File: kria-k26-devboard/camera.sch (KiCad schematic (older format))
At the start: 16 parts, among them J3 WE_68715014522, U60 AP7340-18FS4-7, U9 PI4MSD5V9540BUEX

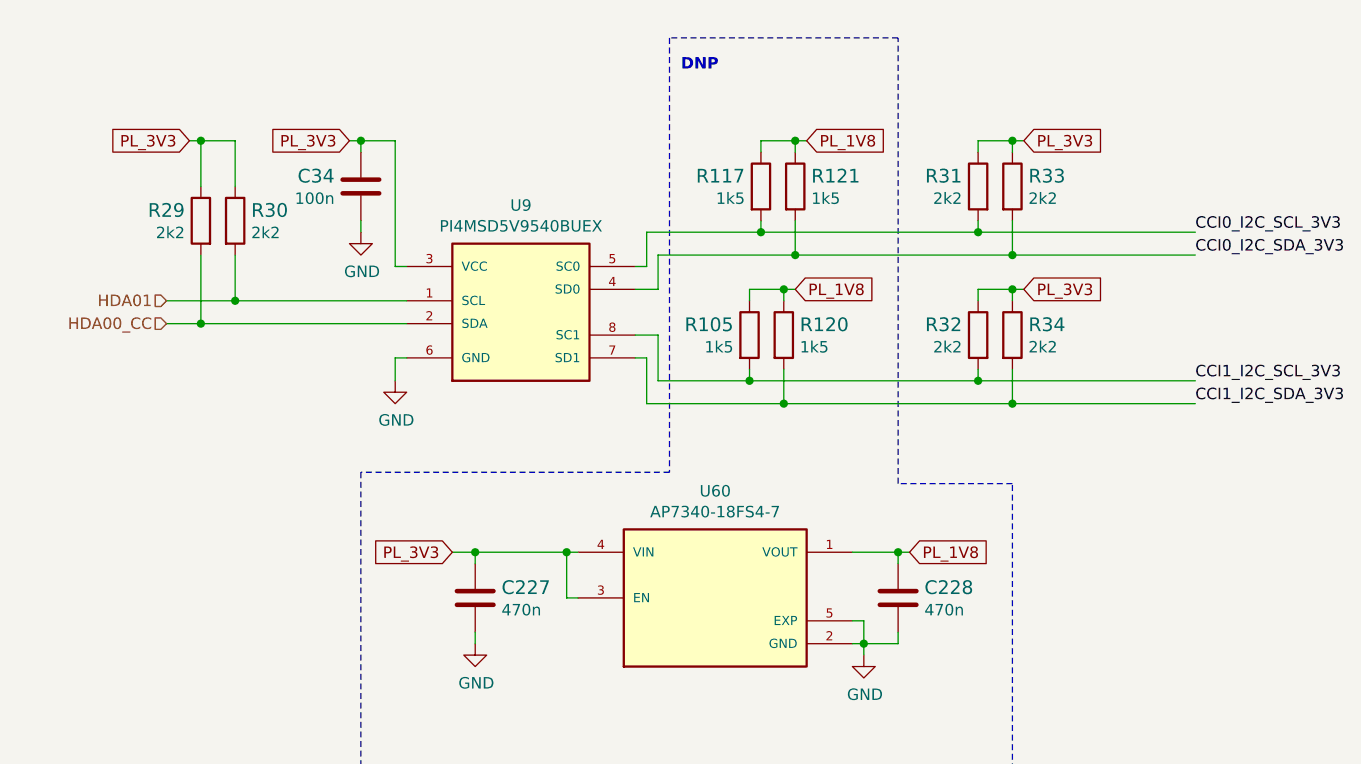
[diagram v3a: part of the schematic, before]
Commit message: Fixed missing USB - M2 connection, finishing touches of PCB
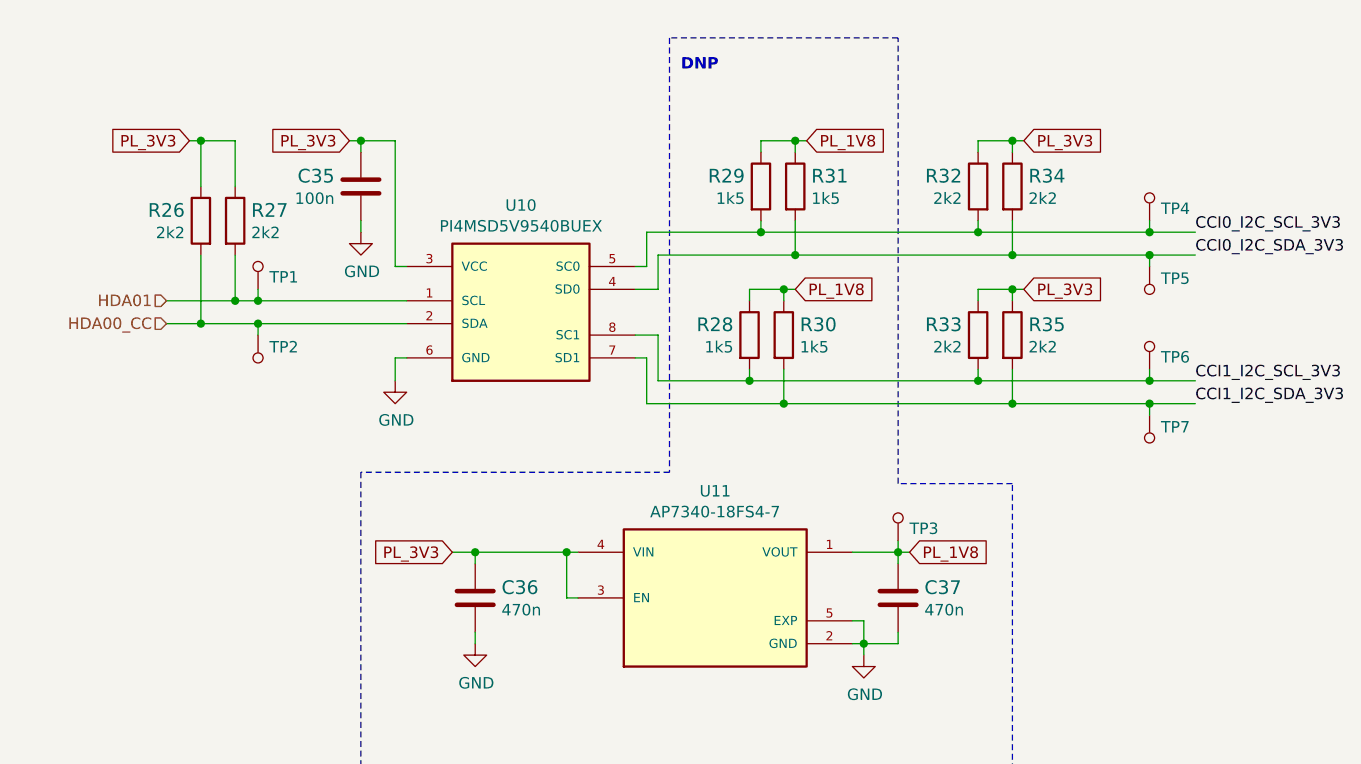
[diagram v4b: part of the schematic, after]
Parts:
- added TP1, TP2, TP3, TP4, TP5, TP6, TP7: TP_SMD_0_75MM, antmicro-footprints:Testpoint_smd_0_75mm, symbol antmicroTestPoints:TP_SMD_0_75MM
- renumbered C34 to C35, C227 to C36, C228 to C37, R29 to R26, R30 to R27, R105 to R28, R117 to R29, R120 to R30, R121 to R31, R31 to R32, R32 to R33, R33 to R34, R34 to R35, U9 to U10, U60 to U11
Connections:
- net CCI0_I2C_SCL_3V3: now also TP4.1
- net CCI0_I2C_SDA_3V3: now also TP5.1
- net CCI1_I2C_SCL_3V3: now also TP6.1
- net CCI1_I2C_SDA_3V3: now also TP7.1
- net HDA00_CC: now also TP2.1
- net HDA01: now also TP1.1
- net PL_1V8: now also TP3.1
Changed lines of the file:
@@
 HPA07_N
 $Comp
-L antmicroLogicSignalSwitchesMultiplexersDecoders:PI4MSD5V9540BUEX U9
+L antmicroLogicSignalSwitchesMultiplexersDecoders:PI4MSD5V9540BUEX U10
 U 1 1 64BDD501
 P 2750 4950
-F 0 "U9" H 2750 5517 50  0000 C CNN
+F 0 "U10" H 2750 5517 50  0000 C CNN
 F 1 "PI4MSD5V9540BUEX" H 2750 5426 50  0000 C CNN
 F 2 "antmicro-footprints:MSOP-8_W3mm_PITCH0.65mm" H 2600 5400 50  0001 L BNN
@@
 	2050 4100 2200 4100
 $Comp
-L power:GND #PWR052
+L power:GND #PWR056
 U 1 1 64C03362
 P 2050 4500
-F 0 "#PWR052" H 2050 4250 50  0001 C CNN
+F 0 "#PWR056" H 2050 4250 50  0001 C CNN
 F 1 "GND" H 2055 4327 50  0000 C CNN
 F 2 "" H 2050 4500 50  0001 C CNN
@@
 	2200 4650 2250 4650
 $Comp
-L power:GND #PWR053
+L power:GND #PWR057
 U 1 1 64C26FC9
 P 2200 5150
-F 0 "#PWR053" H 2200 4900 50  0001 C CNN
+F 0 "#PWR057" H 2200 4900 50  0001 C CNN
 F 1 "GND" H 2205 4977 50  0000 C CNN
 F 2 "" H 2200 5150 50  0001 C CNN
@@
 Connection ~ 1350 4900
 Wire Wire Line
-	1350 4900 2250 4900
+	1350 4900 1600 4900
 Connection ~ 1500 4800
 Wire Wire Line
-	1500 4800 2250 4800
+	1500 4800 1600 4800
 Connection ~ 1350 4100
 Wire Wire Line
@@
 	4750 5100 4750 5150
 $Comp
-L antmicroResistors0402:R_2k2_0402 R34
+L antmicroResistors0402:R_2k2_0402 R35
 U 1 1 649B3ABE
 P 4900 4950
-F 0 "R34" V 4855 5020 60  0000 L CNN
+F 0 "R35" V 4855 5020 60  0000 L CNN
 F 1 "R_2k2_0402" H 4900 4800 60  0001 C CNN
 F 2 "antmicro-footprints:0402-res" H 5100 5150 60  0001 L CNN
@@
 $EndComp
 $Comp
-L antmicroResistors0402:R_2k2_0402 R32
+L antmicroResistors0402:R_2k2_0402 R33
 U 1 1 649A89C1
 P 4750 4950
-F 0 "R32" V 4705 5020 60  0000 L CNN
+F 0 "R33" V 4705 5020 60  0000 L CNN
 F 1 "R_2k2_0402" H 4750 4800 60  0001 C CNN
 F 2 "antmicro-footprints:0402-res" H 4950 5150 60  0001 L CNN
@@
 	4750 4450 4750 4500
 $Comp
-L antmicroResistors0402:R_2k2_0402 R33
+L antmicroResistors0402:R_2k2_0402 R34
 U 1 1 64B09B58
 P 4900 4300
-F 0 "R33" V 4855 4370 60  0000 L CNN
+F 0 "R34" V 4855 4370 60  0000 L CNN
 F 1 "R_2k2_0402" H 4900 4150 60  0001 C CNN
 F 2 "antmicro-footprints:0402-res" H 5100 4500 60  0001 L CNN
@@
 $EndComp
 $Comp
-L antmicroResistors0402:R_2k2_0402 R31
+L antmicroResistors0402:R_2k2_0402 R32
 U 1 1 64B09B4B
 P 4750 4300
-F 0 "R31" V 4705 4370 60  0000 L CNN
+F 0 "R32" V 4705 4370 60  0000 L CNN
 F 1 "R_2k2_0402" H 4750 4150 60  0001 C CNN
 F 2 "antmicro-footprints:0402-res" H 4950 4500 60  0001 L CNN
@@
 PL_3V3
 $Comp
-L antmicroResistors0402:R_2k2_0402 R30
+L antmicroResistors0402:R_2k2_0402 R27
 U 1 1 64DE55BF
 P 1500 4450
-F 0 "R30" V 1455 4520 60  0000 L CNN
+F 0 "R27" V 1455 4520 60  0000 L CNN
 F 1 "R_2k2_0402" H 1500 4300 60  0001 C CNN
 F 2 "antmicro-footprints:0402-res" H 1700 4650 60  0001 L CNN
@@
 $EndComp
 $Comp
-L antmicroResistors0402:R_2k2_0402 R29
+L antmicroResistors0402:R_2k2_0402 R26
 U 1 1 64DE573E
 P 1350 4450
-F 0 "R29" V 1305 4520 60  0000 L CNN
+F 0 "R26" V 1305 4520 60  0000 L CNN
 F 1 "R_2k2_0402" H 1350 4300 60  0001 C CNN
 F 2 "antmicro-footprints:0402-res" H 1550 4650 60  0001 L CNN
@@
 PL_3V3
 $Comp
-L antmicroCapacitors0402:C_100n_0402 C34
+L antmicroCapacitors0402:C_100n_0402 C35
 U 1 1 65AE161E
 P 2050 4300
-F 0 "C34" H 2165 4345 60  0000 L CNN
+F 0 "C35" H 2165 4345 60  0000 L CNN
 F 1 "C_100n_0402" H 2050 4150 60  0001 C CNN
 F 2 "antmicro-footprints:0402-cap" H 2250 4500 60  0001 L CNN
@@
 Camera interface
 $Comp
-L power:GND #PWR0399
+L power:GND #PWR060
 U 1 1 6733CCE5
 P 8350 5800
-F 0 "#PWR0399" H 8350 5550 50  0001 C CNN
+F 0 "#PWR060" H 8350 5550 50  0001 C CNN
 F 1 "GND" H 8355 5627 50  0000 C CNN
 F 2 "" H 8350 5800 50  0001 C CNN
@@
 	3900 5250 4900 5250
 $Comp
-L antmicroResistors0402:R_1k5_0402 R121
+L antmicroResistors0402:R_1k5_0402 R31
 U 1 1 62884B6D
 P 3950 4300
-F 0 "R121" V 3905 4370 60  0000 L CNN
+F 0 "R31" V 3905 4370 60  0000 L CNN
 F 1 "R_1k5_0402" H 3950 4150 60  0001 C CNN
 F 2 "antmicro-footprints:0402-res" H 4150 4500 60  0001 L CNN
@@
 $EndComp
 $Comp
-L antmicroResistors0402:R_1k5_0402 R117
+L antmicroResistors0402:R_1k5_0402 R29
 U 1 1 6288E001
 P 3800 4300
-F 0 "R117" V 3755 4230 60  0000 R CNN
+F 0 "R29" V 3755 4230 60  0000 R CNN
 F 1 "R_1k5_0402" H 3800 4150 60  0001 C CNN
 F 2 "antmicro-footprints:0402-res" H 4000 4500 60  0001 L CNN
@@
 $EndComp
 $Comp
-L antmicroResistors0402:R_1k5_0402 R120
+L antmicroResistors0402:R_1k5_0402 R30
 U 1 1 628A1FB5
 P 3900 4950
-F 0 "R120" V 3855 5020 60  0000 L CNN
+F 0 "R30" V 3855 5020 60  0000 L CNN
 F 1 "R_1k5_0402" H 3900 4800 60  0001 C CNN
 F 2 "antmicro-footprints:0402-res" H 4100 5150 60  0001 L CNN
@@
 $EndComp
 $Comp
-L antmicroResistors0402:R_1k5_0402 R105
+L antmicroResistors0402:R_1k5_0402 R28
 U 1 1 628A2134
 P 3750 4950
-F 0 "R105" V 3705 4880 60  0000 R CNN
+F 0 "R28" V 3705 4880 60  0000 R CNN
 F 1 "R_1k5_0402" H 3750 4800 60  0001 C CNN
 F 2 "antmicro-footprints:0402-res" H 3950 5150 60  0001 L CNN
@@
 DNP
 $Comp
-L antmicroPMICVoltageRegulatorsLinear:AP7340-18FS4-7 U60
+L antmicroPMICVoltageRegulatorsLinear:AP7340-18FS4-7 U11
 U 1 1 62A4CE27
 P 3600 6100
-F 0 "U60" H 3600 6567 50  0000 C CNN
+F 0 "U11" H 3600 6567 50  0000 C CNN
 F 1 "AP7340-18FS4-7" H 3600 6476 50  0000 C CNN
 F 2 "antmicro-footprints:XDFN4" H 3150 5450 50  0001 L BNN
@@
 Connection ~ 2950 5900
 $Comp
-L antmicroCapacitors0402:C_470n_0402 C227
+L antmicroCapacitors0402:C_470n_0402 C36
 U 1 1 62A54360
 P 2550 6100
-F 0 "C227" H 2665 6145 60  0000 L CNN
+F 0 "C36" H 2665 6145 60  0000 L CNN
 F 1 "C_470n_0402" H 2550 5950 60  0001 C CNN
 F 2 "antmicro-footprints:0402-cap" H 2750 6300 60  0001 L CNN
@@
 $EndComp
 $Comp
-L antmicroCapacitors0402:C_470n_0402 C228
+L antmicroCapacitors0402:C_470n_0402 C37
 U 1 1 62A6AE5F
 P 4400 6100
-F 0 "C228" H 4515 6145 60  0000 L CNN
+F 0 "C37" H 4515 6145 60  0000 L CNN
 F 1 "C_470n_0402" H 4400 5950 60  0001 C CNN
 F 2 "antmicro-footprints:0402-cap" H 4600 6300 60  0001 L CNN
@@
 	4200 5900 4400 5900
 $Comp
-L power:GND #PWR0417
+L power:GND #PWR058
 U 1 1 62A87F4F
 P 2550 6300
-F 0 "#PWR0417" H 2550 6050 50  0001 C CNN
+F 0 "#PWR058" H 2550 6050 50  0001 C CNN
 F 1 "GND" H 2555 6127 50  0000 C CNN
 F 2 "" H 2550 6300 50  0001 C CNN
@@
 	4400 6300 4400 6250
 $Comp
-L power:GND #PWR0419
+L power:GND #PWR059
 U 1 1 62A973E6
 P 4250 6350
-F 0 "#PWR0419" H 4250 6100 50  0001 C CNN
+F 0 "#PWR059" H 4250 6100 50  0001 C CNN
 F 1 "GND" H 4255 6177 50  0000 C CNN
 F 2 "" H 4250 6350 50  0001 C CNN
@@
 Connection ~ 4750 4500
 Wire Wire Line
-	4750 4500 5700 4500
+	4750 4500 5500 4500
 Connection ~ 4750 5150
 Wire Wire Line
-	4750 5150 5700 5150
+	4750 5150 5500 5150
 Connection ~ 4900 4600
 Wire Wire Line
-	4900 4600 5700 4600
+	4900 4600 5500 4600
 Connection ~ 4900 5250
 Wire Wire Line
-	4900 5250 5700 5250
+	4900 5250 5500 5250
 Wire Notes Line
 	3400 5550 2050 5550
@@
 Wire Wire Line
 	4250 6350 4250 6300
+$Comp
+L antmicroTestPoints:TP_SMD_0_75MM TP4
+U 1 1 6367AE32
+P 5500 4350
+F 0 "TP4" H 5450 4397 50  0000 R CNN
+F 1 "TP_SMD_0_75MM" H 5500 4250 50  0001 C CNN
+F 2 "antmicro-footprints:Testpoint_smd_0_75mm" H 5700 4550 60  0001 L CNN
+F 3 "" H 5700 4650 60  0001 L CNN
+	1    5500 4350
+	-1   0    0    1
+$EndComp
+$Comp
+L antmicroTestPoints:TP_SMD_0_75MM TP5
+U 1 1 6367BC74
+P 5500 4750
+F 0 "TP5" H 5550 4797 50  0000 L CNN
+F 1 "TP_SMD_0_75MM" H 5500 4650 50  0001 C CNN
+F 2 "antmicro-footprints:Testpoint_smd_0_75mm" H 5700 4950 60  0001 L CNN
+F 3 "" H 5700 5050 60  0001 L CNN
+	1    5500 4750
+	1    0    0    -1
+$EndComp
+$Comp
+L antmicroTestPoints:TP_SMD_0_75MM TP6
+U 1 1 6367C4DB
+P 5500 5000
+F 0 "TP6" H 5450 5047 50  0000 R CNN
+F 1 "TP_SMD_0_75MM" H 5500 4900 50  0001 C CNN
+F 2 "antmicro-footprints:Testpoint_smd_0_75mm" H 5700 5200 60  0001 L CNN
+F 3 "" H 5700 5300 60  0001 L CNN
+	1    5500 5000
+	-1   0    0    1
+$EndComp
+$Comp
+L antmicroTestPoints:TP_SMD_0_75MM TP7
+U 1 1 6367C829
+P 5500 5400
+F 0 "TP7" H 5550 5447 50  0000 L CNN
+F 1 "TP_SMD_0_75MM" H 5500 5300 50  0001 C CNN
+F 2 "antmicro-footprints:Testpoint_smd_0_75mm" H 5700 5600 60  0001 L CNN
+F 3 "" H 5700 5700 60  0001 L CNN
+	1    5500 5400
+	1    0    0    -1
+$EndComp
+Wire Wire Line
+	5500 5300 5500 5250
+Connection ~ 5500 5250
+Wire Wire Line
+	5500 5250 5700 5250
+Wire Wire Line
+	5500 5100 5500 5150
+Connection ~ 5500 5150
+Wire Wire Line
+	5500 5150 5700 5150
+$Comp
+L antmicroTestPoints:TP_SMD_0_75MM TP3
+U 1 1 636882F0
+P 4400 5750
+F 0 "TP3" H 4350 5797 50  0000 R CNN
+F 1 "TP_SMD_0_75MM" H 4400 5650 50  0001 C CNN
+F 2 "antmicro-footprints:Testpoint_smd_0_75mm" H 4600 5950 60  0001 L CNN
+F 3 "" H 4600 6050 60  0001 L CNN
+	1    4400 5750
+	-1   0    0    1
+$EndComp
+Wire Wire Line
+	4400 5900 4400 5850
+$Comp
+L antmicroTestPoints:TP_SMD_0_75MM TP2
+U 1 1 6368ED99
+P 1600 5050
+F 0 "TP2" H 1650 5097 50  0000 L CNN
+F 1 "TP_SMD_0_75MM" H 1600 4950 50  0001 C CNN
+F 2 "antmicro-footprints:Testpoint_smd_0_75mm" H 1800 5250 60  0001 L CNN
+F 3 "" H 1800 5350 60  0001 L CNN
+	1    1600 5050
+	1    0    0    -1
+$EndComp
+$Comp
+L antmicroTestPoints:TP_SMD_0_75MM TP1
+U 1 1 6368F55D
+P 1600 4650
+F 0 "TP1" H 1550 4697 50  0000 R CNN
+F 1 "TP_SMD_0_75MM" H 1600 4550 50  0001 C CNN
+F 2 "antmicro-footprints:Testpoint_smd_0_75mm" H 1800 4850 60  0001 L CNN
+F 3 "" H 1800 4950 60  0001 L CNN
+	1    1600 4650
+	-1   0    0    1
+$EndComp
+Wire Wire Line
+	1600 4750 1600 4800
+Connection ~ 1600 4800
+Wire Wire Line
+	1600 4800 2250 4800
+Wire Wire Line
+	1600 4950 1600 4900
+Connection ~ 1600 4900
+Wire Wire Line
+	1600 4900 2250 4900
+Wire Wire Line
+	5500 4600 5500 4650
+Connection ~ 5500 4600
+Wire Wire Line
+	5500 4600 5700 4600
+Wire Wire Line
+	5500 4500 5500 4450
+Connection ~ 5500 4500
+Wire Wire Line
+	5500 4500 5700 4500
 $EndSCHEMATC

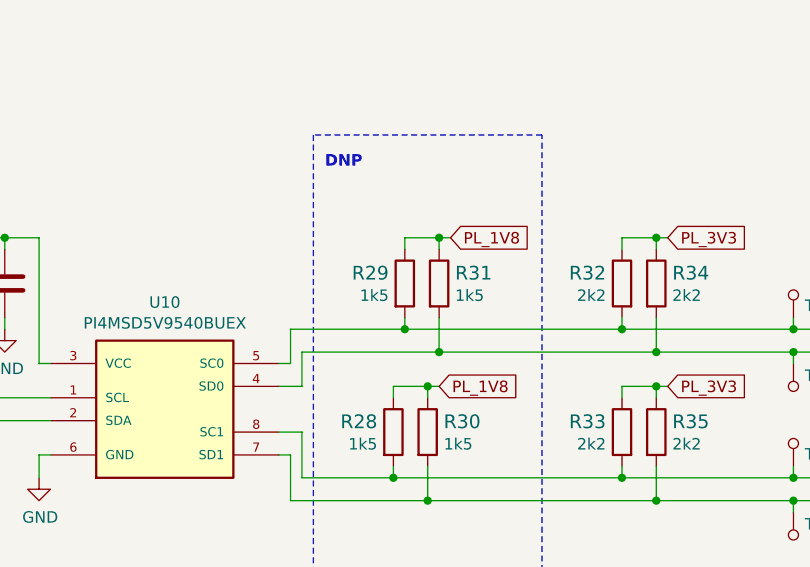
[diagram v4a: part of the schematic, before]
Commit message: Fixes introduced after initial review, length matching double checked with external plugin
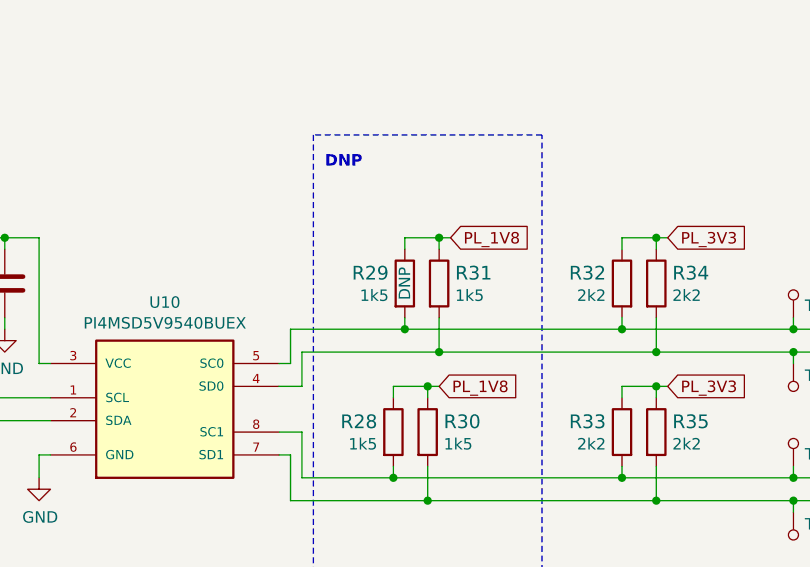
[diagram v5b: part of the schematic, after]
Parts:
- R29: DNP (none) -> DNP
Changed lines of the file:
@@
 $Descr A4 11693 8268
 encoding utf-8
-Sheet 6 19
+Sheet 5 19
 Title ""
 Date "2022-03-10"
@@
 F 5 "MP000515" H 4000 4600 60  0001 L CNN "MPN"
 F 6 "1k5" V 3853 4230 50  0000 R CNN "Val"
+F 7 "DNP" H 3800 4300 50  0000 C CNN "DNP"
 	1    3800 4300
 	0    1    1    0
